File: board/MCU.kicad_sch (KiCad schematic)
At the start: 23 parts, among them SW1 SW_Push, U1 STSPIN32G4TR

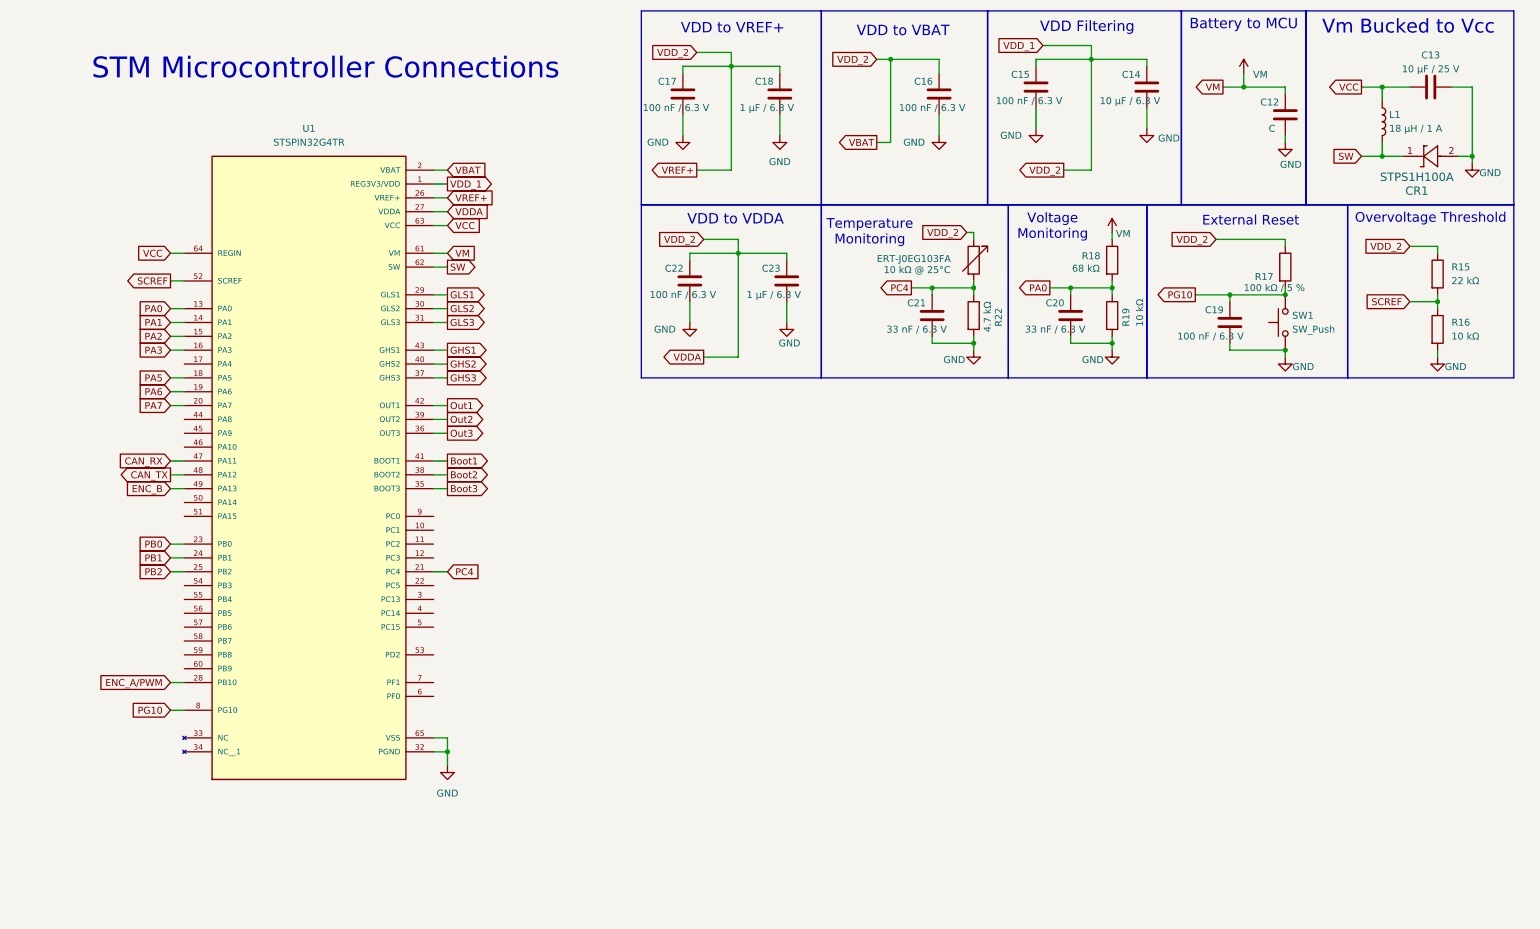
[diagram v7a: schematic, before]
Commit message: Fixed many issues brought up in the schematic review.
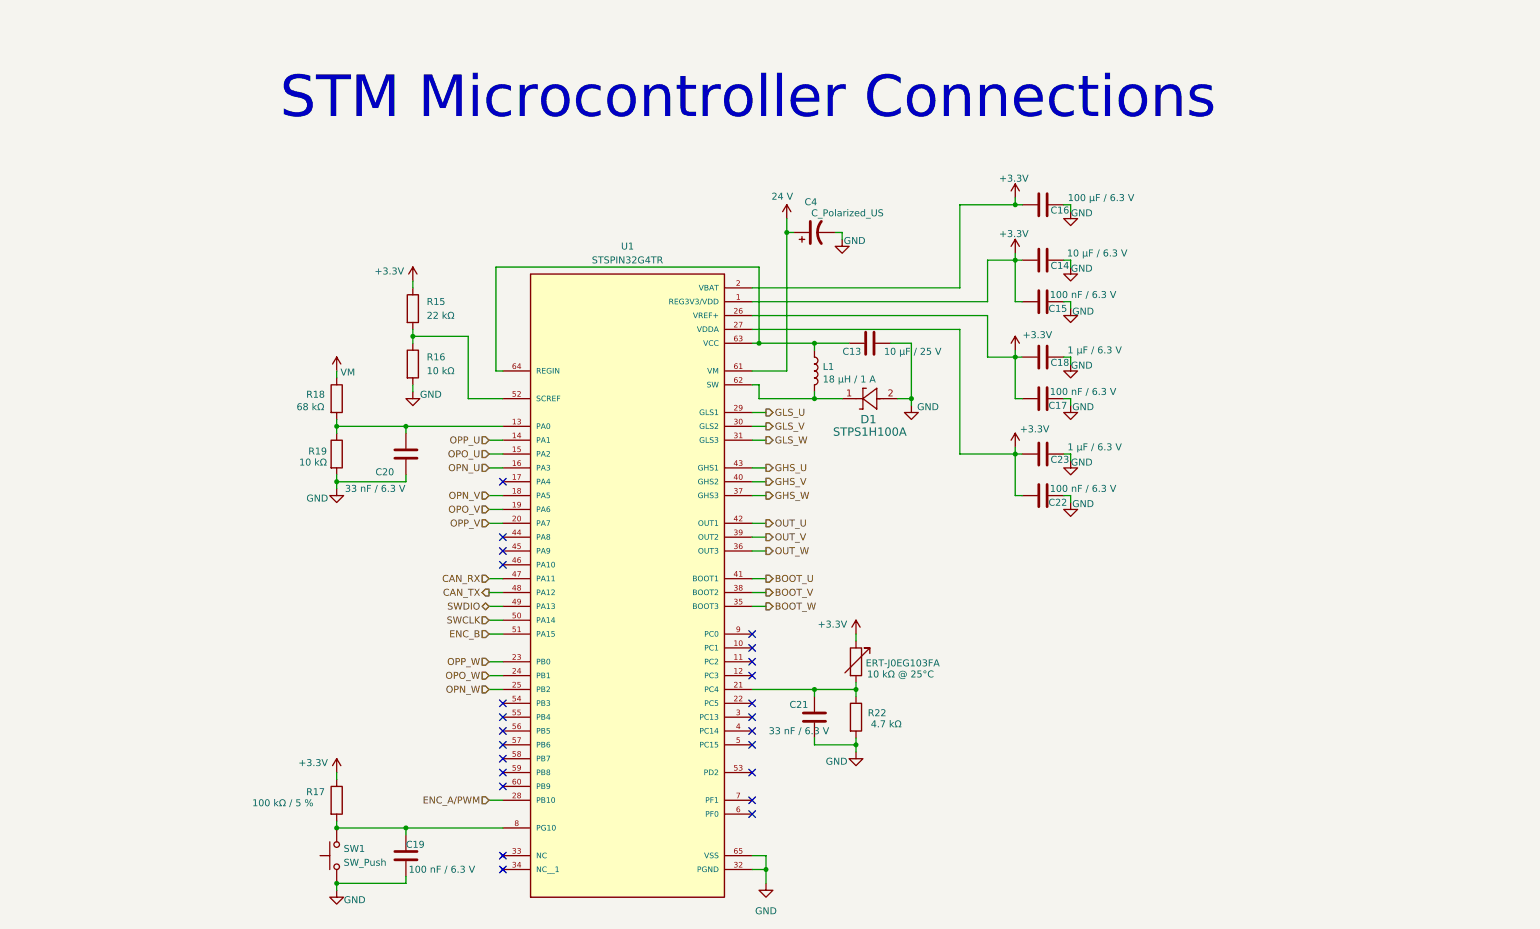
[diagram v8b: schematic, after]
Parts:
- removed C12: C, symbol Device:C
- added C4: C_Polarized_US, symbol Device:C_Polarized_US
- C16: value 100 nF / 6.3 V -> 100 μF / 6.3 V
- STPS1H100A: renamed from CR1; value STPS1H100A -> D1
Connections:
- net ENC_B: now also U1.51 (PA15); no longer U1.49 (PA13)
- net GND: now also C4.2
- net VM: no longer U1.61 (VM)
- net SWCLK: now reaches U1.50 (PA14)
- net Boot1 renamed BOOT_U
- net Boot2 renamed BOOT_V
- net Boot3 renamed BOOT_W
- net GHS1 renamed GHS_U
- net GHS2 renamed GHS_V
- net GHS3 renamed GHS_W
- net GLS1 renamed GLS_U
- net GLS2 renamed GLS_V
- net GLS3 renamed GLS_W
- net Out1 renamed OUT_U
- net Out2 renamed OUT_V
- net Out3 renamed OUT_W
- net PA0: no longer names the net of C20.1, R18.2, R19.1, U1.13 (PA0)
- net PA1 renamed OPP_U
- net PA2 renamed OPO_U
- net PA3 renamed OPN_U
- net PA5 renamed OPN_V
- net PA6 renamed OPO_V
- net PA7 renamed OPP_V
- net PB0 renamed OPP_W
- net PB1 renamed OPO_W
- net PB2 renamed OPN_W
- net PC4: no longer names the net of C21.1, ERT-J0EG103FA.2, R22.1, U1.21 (PC4)
- net PG10: no longer names the net of C19.1, R17.2, SW1.2, U1.8 (PG10)
- net SCREF: no longer names the net of R15.2, R16.1, U1.52 (SCREF)
- net SW: no longer names the net of L1.2, STPS1H100A.1, U1.62 (SW)
- net VBAT renamed +3.3V
- net VCC: no longer names the net of C13.1, L1.1, U1.63 (VCC), U1.64 (REGIN)
- new net 24 V: C4.1, U1.61 (VM)
- new net SWDIO: U1.49 (PA13)
- no-connect marks 0 -> 24
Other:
- note removed: "Battery to MCU"
- note removed: "External Reset"
- note removed: "Overvoltage Threshold"
- note removed: "Temperature Monitoring"
- note removed: "VDD Filtering"
- note removed: "VDD to VBAT"
- note removed: "VDD to VDDA"
- note removed: "VDD to VREF+"
- note removed: "Vm Bucked to Vcc"
- note removed: "Voltage Monitoring"
- moved on the sheet: C13, C19, C20, C21, C22, C23, ERT-J0EG103FA, L1, R15, R16, R17, R18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
